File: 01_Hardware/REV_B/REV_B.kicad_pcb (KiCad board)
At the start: 2 copper layers, 65 x 30.5 mm, 6 parts, among them J1 Conn_02x20_Odd_Even, J2 RPi_GPIO, U1 MCP3004, U2 TB6612FNG

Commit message: Designing RevB
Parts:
- removed ? (x2): , RPi_Hat:RPi_Hat_Mounting_Hole
- added 100n1: C, Capacitor_SMD:C_0603_1608Metric, F.Cu at (44.2, 49.6)
- added C1: 10n, Capacitor_SMD:C_0603_1608Metric, F.Cu at (43.2, 65.6)
- added C10: 100n, Capacitor_SMD:C_0603_1608Metric, F.Cu at (25.6, 68.0)
- added C2: 10n, Capacitor_SMD:C_0603_1608Metric, F.Cu at (39.8, 65.6)
- added C3: 10n, Capacitor_SMD:C_0603_1608Metric, F.Cu at (21.8, 62.7)
- added C4: 10n, Capacitor_SMD:C_0603_1608Metric, F.Cu at (31.6, 59.3)
- added C5: 10n, Capacitor_SMD:C_0603_1608Metric, F.Cu at (43.3, 44.2)
- added C6: 10n, Capacitor_SMD:C_0603_1608Metric, F.Cu at (39.9, 49.6)
- added C7: 10n, Capacitor_SMD:C_0603_1608Metric, F.Cu at (25.1, 62.7)
- added C8: 10n, Capacitor_SMD:C_0603_1608Metric, F.Cu at (21.8, 68.0)
- added C9: 10u, Capacitor_SMD:CP_Elec_4x4.5, F.Cu at (33.5, 40.0)
- added J3: Conn_01x02, Connector_Molex:Molex_KK-254_AE-6410-02A_1x02_P2.54mm_Vertical, F.Cu at (61.2, 22.4)
- added J4: Conn_01x08_Male, Connector_PinHeader_2.54mm:PinHeader_1x08_P2.54mm_Vertical, F.Cu at (23.0, 38.8)
- added J5: Conn_01x08_Male, Connector_PinHeader_2.54mm:PinHeader_1x08_P2.54mm_Vertical, F.Cu at (9.20, 38.8)
- added R1: 10k, Resistor_SMD:R_0603_1608Metric, F.Cu at (53.5, 54.9)
- added R10: 1k, Resistor_SMD:R_0603_1608Metric, F.Cu at (32.9, 64.7)
- added R11: 1k, Resistor_SMD:R_0603_1608Metric, F.Cu at (58.7, 38.2)
- added R12: 1k, Resistor_SMD:R_0603_1608Metric, F.Cu at (39.9, 44.2)
- added R13: 1k, Resistor_SMD:R_0603_1608Metric, F.Cu at (69.1, 38.2)
- added R14: 22k, Resistor_SMD:R_0603_1608Metric, F.Cu at (38.4, 60.3)
- added R15: 22k, Resistor_SMD:R_0603_1608Metric, F.Cu at (41.9, 60.3)
- added R16: 22k, Resistor_SMD:R_0603_1608Metric, F.Cu at (32.9, 70.0)
- added R17: 22k, Resistor_SMD:R_0603_1608Metric, F.Cu at (52.0, 49.6)
- added R18: 10k, Resistor_SMD:R_0603_1608Metric, F.Cu at (46.7, 54.9)
- added R19: 10k, Resistor_SMD:R_0603_1608Metric, F.Cu at (62.2, 38.2)
- added R2: 1k, Resistor_SMD:R_0603_1608Metric, F.Cu at (46.7, 44.2)
- added R20: 10k, Resistor_SMD:R_0603_1608Metric, F.Cu at (56.9, 43.5)
- added R21: 10k, Resistor_SMD:R_0603_1608Metric, F.Cu at (60.3, 43.5)
- added R22: 10k, Resistor_SMD:R_0603_1608Metric, F.Cu at (65.6, 38.2)
- added R23: 10k, Resistor_SMD:R_0603_1608Metric, F.Cu at (36.4, 65.6)
- added R24: 10k, Resistor_SMD:R_0603_1608Metric, F.Cu at (29.5, 70.0)
- added R25: 10k, Resistor_SMD:R_0603_1608Metric, F.Cu at (36.4, 71.0)
- added R26: 10k, Resistor_SMD:R_0603_1608Metric, F.Cu at (48.6, 49.6)
- added R27: 10k, Resistor_SMD:R_0603_1608Metric, F.Cu at (63.8, 43.5)
- added R28: 10k, Resistor_SMD:R_0603_1608Metric, F.Cu at (56.9, 48.9)
- added R29: 10k, Resistor_SMD:R_0603_1608Metric, F.Cu at (50.1, 54.9)
- added R3: 1k, Resistor_SMD:R_0603_1608Metric, F.Cu at (55.3, 38.2)
- added R30: 10k, Resistor_SMD:R_0603_1608Metric, F.Cu at (45.3, 60.3)
- added R31: 10k, Resistor_SMD:R_0603_1608Metric, F.Cu at (60.3, 48.9)
- added R32: 10k, Resistor_SMD:R_0603_1608Metric, F.Cu at (48.8, 60.3)
- added R4: 1k, Resistor_SMD:R_0603_1608Metric, F.Cu at (29.5, 64.7)
- added R5: 1k, Resistor_SMD:R_0603_1608Metric, F.Cu at (50.1, 44.2)
- added R6: 10k, Resistor_SMD:R_0603_1608Metric, F.Cu at (39.9, 54.9)
- added R7: 10k, Resistor_SMD:R_0603_1608Metric, F.Cu at (35.0, 59.3)
- added R8: 10k, Resistor_SMD:R_0603_1608Metric, F.Cu at (43.3, 54.9)
- added R9: 10k, Resistor_SMD:R_0603_1608Metric, F.Cu at (53.5, 44.2)
- added U3: BSS138PS, Package_TO_SOT_SMD:SOT-363_SC-70-6, F.Cu at (34.1, 53.6)
- added U4: BSS138PS, Package_TO_SOT_SMD:SOT-363_SC-70-6, F.Cu at (34.1, 47.6)
- added U5: BSS138PS, Package_TO_SOT_SMD:SOT-363_SC-70-6, F.Cu at (41.2, 38.5)
- added U6: MCP3008, Package_SOIC:SOIC-16_3.9x9.9mm_P1.27mm, F.Cu at (6.21, 67.0)
- J1: value Conn_02x20_Odd_Even -> RaspberryPi; footprint Connector_PinHeader_2.54mm:PinHeader_2x20_P2.54mm_Vertical -> Connector_PinSocket_2.54mm:PinSocket_2x20_P2.54mm_Vertical
- J2: value RPi_GPIO -> Conn_01x02; footprint RPi_Hat:Pin_Header_Straight_2x20 -> Connector_Molex:Molex_KK-254_AE-6410-02A_1x02_P2.54mm_Vertical
- U1: value MCP3004 -> TB6612FNG; footprint Package_SSOP:TSSOP-14_4.4x5mm_P0.65mm -> Package_SSOP:SSOP-24_5.3x8.2mm_P0.65mm
- U2: value TB6612FNG -> BSS138PS; footprint Package_SSOP:SSOP-24_5.3x8.2mm_P0.65mm -> Package_TO_SOT_SMD:SOT-363_SC-70-6
- moved J1 140.6 mm to (8.37, 2.28)
- moved U2 127.6 mm to (49.5, 38.5)
- moved U1 107.9 mm to (15.1, 66.3)
- moved J2 105.9 mm to (61.2, 14.5), turned to 270 degrees
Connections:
- J1 pad 10: /GPIO15 -> Net-(J1-Pad10)
- J1 pad 11: /GPIO17 -> Net-(J1-Pad11)
- J1 pad 12: /GPIO18 -> Net-(J1-Pad12)
- J1 pad 13: /GPIO27 -> Net-(J1-Pad13)
- J1 pad 15: /GPIO22 -> Net-(J1-Pad15)
- J1 pad 16: /GPIO23 -> Net-(J1-Pad16)
- J1 pad 18: /GPIO24 -> Net-(J1-Pad18)
- J1 pad 19: /GPIO10 -> Net-(J1-Pad19)
- J1 pad 21: /GPIO9 -> Net-(J1-Pad21)
- J1 pad 22: /GPIO25 -> Net-(J1-Pad22)
- J1 pad 23: /GPIO11 -> Net-(J1-Pad23)
- J1 pad 24: /GPIO8 -> Net-(J1-Pad24)
- J1 pad 26: /GPIO7 -> Net-(J1-Pad26)
- J1 pad 27: (no net) -> Net-(J1-Pad27)
- J1 pad 28: (no net) -> Net-(J1-Pad28)
- J1 pad 29: /GPIO5 -> Net-(J1-Pad29)
- J1 pad 3: /GPIO2 -> IC21_SDA
- J1 pad 31: /GPIO6 -> Net-(J1-Pad31)
- J1 pad 32: /GPIO12 -> Net-(J1-Pad32)
- J1 pad 33: /GPIO13 -> Net-(J1-Pad33)
- J1 pad 35: /GPIO19 -> Net-(J1-Pad35)
- J1 pad 36: /GPIO16 -> Net-(J1-Pad36)
- J1 pad 37: /GPIO26 -> Net-(J1-Pad37)
- J1 pad 38: /GPIO20 -> Net-(J1-Pad38)
- J1 pad 40: /GPIO21 -> Net-(J1-Pad40)
- J1 pad 5: /GPIO3 -> I2C1_SCL
- J1 pad 7: /GPIO4 -> Net-(J1-Pad7)
- J1 pad 8: /GPIO14 -> Net-(J1-Pad8)
- J2 pad 1: +3V3 -> Net-(J2-Pad1)
- J2 pad 2: +5V -> Net-(J2-Pad2)
- U1 pad 1: (no net) -> Net-(J2-Pad1)
- U1 pad 10: (no net) -> GND
- U1 pad 11: (no net) -> Net-(J3-Pad1)
- U1 pad 12: (no net) -> Net-(J3-Pad1)
- U1 pad 13: (no net) -> +BATT
- U1 pad 14: (no net) -> +BATT
- U1 pad 2: (no net) -> Net-(J2-Pad1)
- U1 pad 3: (no net) -> GND
- U1 pad 4: (no net) -> GND
- U1 pad 5: (no net) -> Net-(J2-Pad2)
- U1 pad 6: (no net) -> Net-(J2-Pad2)
- U1 pad 7: (no net) -> Net-(J3-Pad2)
- U1 pad 8: (no net) -> Net-(J3-Pad2)
- U1 pad 9: (no net) -> GND
- U2 pad 1: (no net) -> IC21_SDA
- U2 pad 2: (no net) -> +3V3
- U2 pad 3: (no net) -> Net-(J5-Pad2)
- U2 pad 4: (no net) -> I2C1_SCL
- U2 pad 5: (no net) -> +3V3
- U2 pad 6: (no net) -> Net-(J5-Pad1)
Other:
- board size 65 x 30.5 mm -> 65 x 30 mm
- net class Default: via_dia 0.6 -> 0.8
- rule pad_to_mask_clearance: 0 -> 0.2
- rule trace_min: 0.01 -> 0.2

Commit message: Work in Progress
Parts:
- removed U4: BSS138PS, Package_TO_SOT_SMD:SOT-363_SC-70-6
- added J10: Conn_01x03, Connector_PinHeader_2.54mm:PinHeader_1x03_P2.54mm_Vertical, F.Cu at (36.8, 21.8)
- added J11: Conn_01x03, Connector_PinHeader_2.54mm:PinHeader_1x03_P2.54mm_Vertical, F.Cu at (54.9, -19.8)
- added J12: Conn_01x03, Connector_PinHeader_2.54mm:PinHeader_1x03_P2.54mm_Vertical, F.Cu at (48.3, 21.8)
- added J13: Conn_01x03, Connector_PinHeader_2.54mm:PinHeader_1x03_P2.54mm_Vertical, F.Cu at (51.8, 21.8)
- added J14: Conn_01x03, Connector_PinHeader_2.54mm:PinHeader_1x03_P2.54mm_Vertical, F.Cu at (55.4, 21.8)
- added J15: Conn_01x03, Connector_PinHeader_2.54mm:PinHeader_1x03_P2.54mm_Vertical, F.Cu at (40.4, 21.8)
- added J16: Conn_01x08_Male, Connector_PinHeader_2.54mm:PinHeader_1x03_P2.54mm_Vertical, F.Cu at (43.9, 21.8)
- added J6: Conn_01x03, Connector_PinHeader_2.54mm:PinHeader_1x03_P2.54mm_Vertical, F.Cu at (22.4, 21.8)
- added J7: Conn_01x03, Connector_PinHeader_2.54mm:PinHeader_1x03_P2.54mm_Vertical, F.Cu at (25.7, 21.8)
- added J8: Conn_01x03, Connector_PinHeader_2.54mm:PinHeader_1x03_P2.54mm_Vertical, F.Cu at (29.2, 21.8)
- added J9: Conn_01x03, Connector_PinHeader_2.54mm:PinHeader_1x03_P2.54mm_Vertical, F.Cu at (33.3, 21.8)
- added U7: BSS138PS, Package_SSOP:TSSOP-28_4.4x9.7mm_P0.65mm, B.Cu at (41.7, 14.5)
- added U8: BSS138PS, Package_TO_SOT_SMD:SOT-363_SC-70-6, F.Cu at (63.8, -20.2)
- C1: value 10n -> 10u
- C10: value 100n -> 10n
- C2: value 10n -> 100n
- C9: value 10u -> 10n
- J4: value Conn_01x08_Male -> Conn_01x02
- R1, R9: value 10k -> 1k
- R13: value 1k -> 22k
- R17: value 22k -> 10k
- R5: value 1k -> 10k
- U2: value BSS138PS -> MCP3008
- U3: value BSS138PS -> PCA9685PW
- U6: value MCP3008 -> BSS138PS
- moved R16 79.4 mm to (70.1, -0.14), turned to 90 degrees
- moved C8 75.6 mm to (76.7, 16.0), turned to 90 degrees
- moved C10 75.0 mm to (76.6, 13.0), turned to 90 degrees
- moved R15 70.7 mm to (72.5, -3.51), turned to 90 degrees
- moved C3 69.9 mm to (74.6, 16.8), turned to 90 degrees
- moved C7 69.8 mm to (74.6, 13.5), turned to 90 degrees
- moved R14 69.3 mm to (72.5, -0.06), turned to 90 degrees
- moved R7 67.5 mm to (72.3, 3.10), turned to 90 degrees
- moved C4 66.7 mm to (72.3, 6.47), turned to 90 degrees
- moved R25 64.9 mm to (6.22, 13.5), turned to 180 degrees
- moved R30 63.4 mm to (6.22, 10.4), turned to 180 degrees
- moved R27 62.4 mm to (6.22, 19.3), turned to 180 degrees
- moved U1 61.6 mm to (47.8, 14.0), turned to 180 degrees
- moved R4 61.0 mm to (74.6, 23.6), turned to 90 degrees
- moved R10 61.0 mm to (74.6, 20.2), turned to 90 degrees
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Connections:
- C1 pad 1: Net-(C1-Pad1) -> +BATT
- C10 pad 1: +BATT -> Net-(C10-Pad1)
- C2 pad 1: Net-(C2-Pad1) -> +BATT
- C9 pad 1: +BATT -> Net-(C9-Pad1)
- J1 pad 10: Net-(J1-Pad10) -> (no net)
- J1 pad 11: Net-(J1-Pad11) -> (no net)
- J1 pad 12: Net-(J1-Pad12) -> (no net)
- J1 pad 13: Net-(J1-Pad13) -> (no net)
- J1 pad 15: Net-(J1-Pad15) -> (no net)
- J1 pad 16: Net-(J1-Pad16) -> (no net)
- J1 pad 18: Net-(J1-Pad18) -> (no net)
- J1 pad 19: Net-(J1-Pad19) -> (no net)
- J1 pad 21: Net-(J1-Pad21) -> (no net)
- J1 pad 22: Net-(J1-Pad22) -> (no net)
- J1 pad 23: Net-(J1-Pad23) -> (no net)
- J1 pad 24: Net-(J1-Pad24) -> (no net)
- J1 pad 26: Net-(J1-Pad26) -> (no net)
- J1 pad 27: Net-(J1-Pad27) -> (no net)
- J1 pad 28: Net-(J1-Pad28) -> (no net)
- J1 pad 29: Net-(J1-Pad29) -> (no net)
- J1 pad 3: IC21_SDA -> (no net)
- J1 pad 31: Net-(J1-Pad31) -> (no net)
- J1 pad 5: I2C1_SCL -> (no net)
- J1 pad 7: Net-(J1-Pad7) -> (no net)
- J1 pad 8: Net-(J1-Pad8) -> (no net)
- J2 pad 1: Net-(J2-Pad1) -> +BATT
- J2 pad 2: Net-(J2-Pad2) -> GND
- J4 pad 3: Net-(J4-Pad3) -> (no net)
- J4 pad 4: Net-(J4-Pad4) -> (no net)
- J4 pad 5: Net-(J4-Pad5) -> (no net)
- J4 pad 6: Net-(J4-Pad6) -> (no net)
- J4 pad 7: Net-(J4-Pad7) -> (no net)
- J4 pad 8: Net-(J4-Pad8) -> (no net)
- R1 pad 1: +3V3 -> Net-(C3-Pad1)
- R1 pad 2: Net-(R1-Pad2) -> GND
- R10 pad 1: Net-(J4-Pad1) -> Net-(J5-Pad2)
- R10 pad 2: Net-(C1-Pad1) -> Net-(C4-Pad1)
- R11 pad 1: Net-(J4-Pad2) -> Net-(J5-Pad3)
- R11 pad 2: Net-(C2-Pad1) -> Net-(C5-Pad1)
- R12 pad 1: Net-(J4-Pad3) -> Net-(J5-Pad4)
- R12 pad 2: Net-(C3-Pad1) -> Net-(C6-Pad1)
- R13 pad 1: Net-(J4-Pad4) -> Net-(J5-Pad5)
- R13 pad 2: Net-(C4-Pad1) -> Net-(C7-Pad1)
- R14 pad 1: Net-(J4-Pad5) -> Net-(J5-Pad6)
- R14 pad 2: Net-(C5-Pad1) -> Net-(C8-Pad1)
- R15 pad 1: Net-(J4-Pad6) -> Net-(J5-Pad7)
- R15 pad 2: Net-(C6-Pad1) -> Net-(C9-Pad1)
- R16 pad 1: Net-(J4-Pad7) -> Net-(J5-Pad8)
- R16 pad 2: Net-(C7-Pad1) -> Net-(C10-Pad1)
- R17 pad 1: Net-(J4-Pad8) -> +3V3
- R17 pad 2: Net-(C8-Pad1) -> Net-(R17-Pad2)
- R19 pad 2: IC21_SDA -> Net-(R19-Pad2)
- R2 pad 1: Net-(C1-Pad1) -> Net-(C4-Pad1)
- R20 pad 2: I2C1_SCL -> Net-(R20-Pad2)
- R25 pad 2: Net-(J5-Pad3) -> Net-(J16-Pad3)
- R26 pad 2: Net-(J5-Pad1) -> Net-(J16-Pad1)
- R27 pad 2: Net-(J5-Pad5) -> Net-(J16-Pad5)
- R28 pad 2: Net-(J5-Pad7) -> Net-(J16-Pad7)
- R29 pad 2: Net-(J5-Pad4) -> Net-(J16-Pad4)
- R3 pad 1: Net-(C2-Pad1) -> Net-(C5-Pad1)
- R30 pad 2: Net-(J5-Pad2) -> Net-(J16-Pad2)
- R31 pad 2: Net-(J5-Pad6) -> Net-(J16-Pad6)
- R32 pad 2: Net-(J5-Pad8) -> Net-(J16-Pad8)
- R4 pad 1: Net-(C3-Pad1) -> Net-(C6-Pad1)
- R5 pad 1: Net-(C4-Pad1) -> Net-(C7-Pad1)
- R6 pad 1: Net-(C5-Pad1) -> Net-(C8-Pad1)
- R7 pad 1: Net-(C6-Pad1) -> Net-(C9-Pad1)
- R8 pad 1: Net-(C7-Pad1) -> Net-(C10-Pad1)
- R9 pad 1: Net-(C8-Pad1) -> Net-(J5-Pad1)
- R9 pad 2: GND -> Net-(C3-Pad1)
- U1 pad 1: Net-(J2-Pad1) -> Net-(J3-Pad1)
- U1 pad 11: Net-(J3-Pad1) -> Net-(J4-Pad1)
- U1 pad 12: Net-(J3-Pad1) -> Net-(J4-Pad1)
- U1 pad 2: Net-(J2-Pad1) -> Net-(J3-Pad1)
- U1 pad 5: Net-(J2-Pad2) -> Net-(J3-Pad2)
- U1 pad 6: Net-(J2-Pad2) -> Net-(J3-Pad2)
- U1 pad 7: Net-(J3-Pad2) -> Net-(J4-Pad2)
- U1 pad 8: Net-(J3-Pad2) -> Net-(J4-Pad2)
- U2 pad 1: IC21_SDA -> Net-(C3-Pad1)
- U2 pad 2: +3V3 -> Net-(C4-Pad1)
- U2 pad 3: Net-(J5-Pad2) -> Net-(C5-Pad1)
- U2 pad 4: I2C1_SCL -> Net-(C6-Pad1)
- U2 pad 5: +3V3 -> Net-(C7-Pad1)
- U2 pad 6: Net-(J5-Pad1) -> Net-(C8-Pad1)
- U3 pad 1: Net-(R1-Pad2) -> (no net)
- U3 pad 2: +3V3 -> (no net)
- U3 pad 3: Net-(J5-Pad4) -> (no net)
- U3 pad 4: Net-(R18-Pad2) -> (no net)
- U3 pad 5: +3V3 -> (no net)
- U3 pad 6: Net-(J5-Pad3) -> Net-(J6-Pad1)
- U5 pad 1: Net-(R23-Pad2) -> Net-(R17-Pad2)
- U5 pad 3: Net-(J5-Pad8) -> Net-(J16-Pad4)
- U5 pad 4: Net-(R24-Pad2) -> Net-(R18-Pad2)
- U5 pad 6: Net-(J5-Pad7) -> Net-(J16-Pad3)
- U6 pad 1: Net-(C1-Pad1) -> Net-(R19-Pad2)
- U6 pad 10: Net-(J1-Pad24) -> (no net)
- U6 pad 11: Net-(J1-Pad19) -> (no net)
- U6 pad 12: Net-(J1-Pad21) -> (no net)
- U6 pad 13: Net-(J1-Pad23) -> (no net)
- U6 pad 14: GND -> (no net)
- U6 pad 15: +3V3 -> (no net)
- U6 pad 16: +3V3 -> (no net)
- U6 pad 2: Net-(C2-Pad1) -> +3V3
- U6 pad 3: Net-(C3-Pad1) -> Net-(J16-Pad2)
- U6 pad 4: Net-(C4-Pad1) -> Net-(R20-Pad2)
- U6 pad 5: Net-(C5-Pad1) -> +3V3
- U6 pad 6: Net-(C6-Pad1) -> Net-(J16-Pad1)
- U6 pad 7: Net-(C7-Pad1) -> (no net)
- U6 pad 8: Net-(C8-Pad1) -> (no net)
- U6 pad 9: GND -> (no net)
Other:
- board text added: "x = 8,37 y = 2,278"

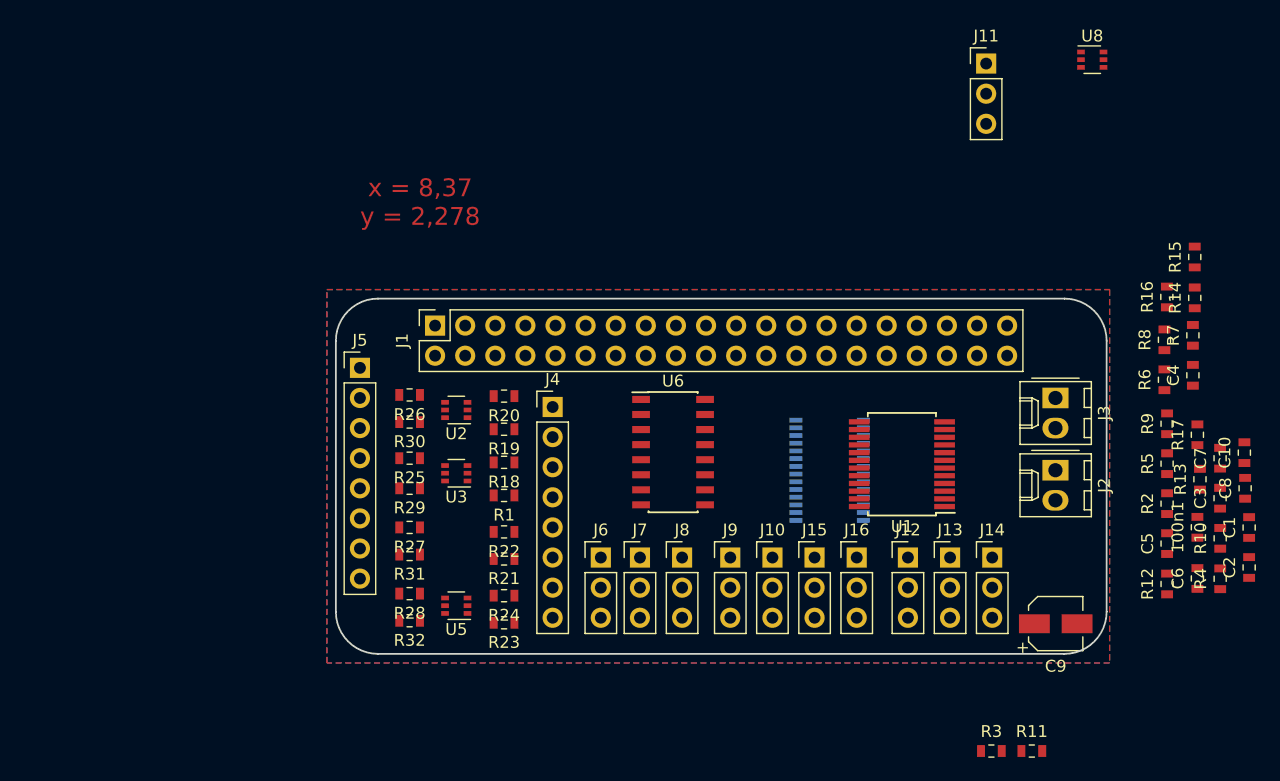
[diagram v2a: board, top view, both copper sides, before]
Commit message: Brd redo due to kicad update
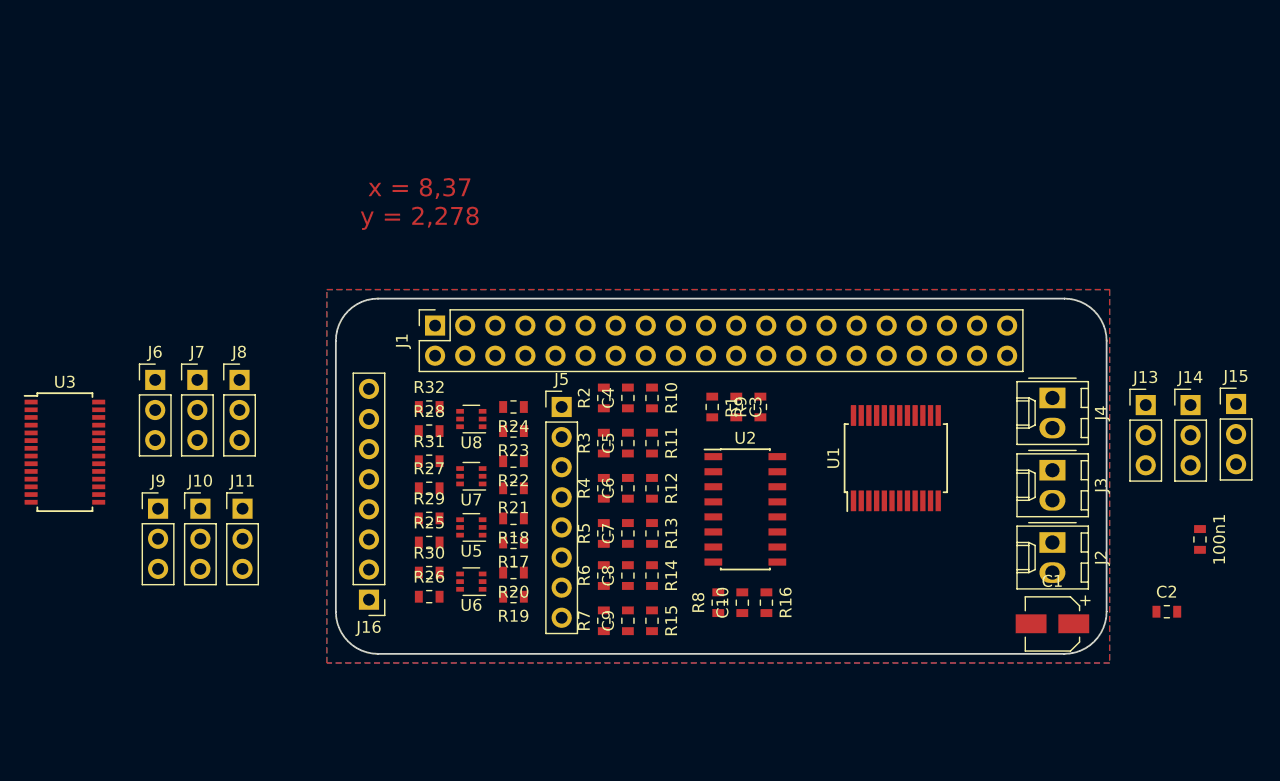
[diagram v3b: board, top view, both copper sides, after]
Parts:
- removed J12: Conn_01x03, Connector_PinHeader_2.54mm:PinHeader_1x03_P2.54mm_Vertical
- C1: footprint Capacitor_SMD:C_0603_1608Metric -> Capacitor_SMD:CP_Elec_4x4.5
- C9: footprint Capacitor_SMD:CP_Elec_4x4.5 -> Capacitor_SMD:C_0603_1608Metric
- J16: footprint Connector_PinHeader_2.54mm:PinHeader_1x03_P2.54mm_Vertical -> Connector_PinHeader_2.54mm:PinHeader_1x08_P2.54mm_Vertical
- J4: footprint Connector_PinHeader_2.54mm:PinHeader_1x08_P2.54mm_Vertical -> Connector_Molex:Molex_KK-254_AE-6410-02A_1x02_P2.54mm_Vertical
- U1: footprint Package_SSOP:SSOP-24_5.3x8.2mm_P0.65mm -> Package_SO:SSOP-24_5.3x8.2mm_P0.65mm
- U2: footprint Package_TO_SOT_SMD:SOT-363_SC-70-6 -> Package_SO:SOIC-16_3.9x9.9mm_P1.27mm
- U3: footprint Package_TO_SOT_SMD:SOT-363_SC-70-6 -> Package_SO:TSSOP-28_4.4x9.7mm_P0.65mm
- U6: footprint Package_SOIC:SOIC-16_3.9x9.9mm_P1.27mm -> Package_TO_SOT_SMD:SOT-363_SC-70-6
- U7: footprint Package_SSOP:TSSOP-28_4.4x9.7mm_P0.65mm -> Package_TO_SOT_SMD:SOT-363_SC-70-6; moved to F.Cu
- moved J11 73.1 mm to (-7.87, 17.7)
- moved U8 60.5 mm to (11.4, 10.2), turned to 180 degrees
- moved R17 58.4 mm to (15.0, 20.6), turned to 180 degrees
- moved R7 55.2 mm to (22.6, 27.2)
- moved R15 55.1 mm to (26.7, 27.2), turned to 270 degrees
- moved C8 52.6 mm to (24.6, 23.4)
- moved R4 52.6 mm to (22.6, 16.0)
- moved R14 51.4 mm to (26.7, 23.4), turned to 270 degrees
- moved C7 50.4 mm to (24.6, 19.8)
- moved R6 50.1 mm to (22.6, 23.4)
- moved R10 49.4 mm to (26.7, 8.38), turned to 270 degrees
- moved C6 48.6 mm to (24.6, 16.0)
- moved J9 48.4 mm to (-15.0, 17.7)
- moved J10 48.4 mm to (-11.4, 17.7)
- moved R2 48.3 mm to (22.6, 8.38)
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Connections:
- J1 pad 19: (no net) -> Net-(J1-Pad19)
- J1 pad 21: (no net) -> Net-(J1-Pad21)
- J1 pad 23: (no net) -> Net-(J1-Pad23)
- J1 pad 24: (no net) -> Net-(J1-Pad24)
- J1 pad 38: Net-(J1-Pad38) -> (no net)
- J10 pad 1: (no net) -> Net-(J10-Pad1)
- J11 pad 1: (no net) -> Net-(J11-Pad1)
- J6 pad 2: (no net) -> Net-(J6-Pad2)
- J6 pad 3: (no net) -> Net-(J6-Pad3)
- J7 pad 1: (no net) -> Net-(J7-Pad1)
- J7 pad 2: (no net) -> Net-(J7-Pad2)
- J7 pad 3: (no net) -> Net-(J7-Pad3)
- J8 pad 1: (no net) -> Net-(J8-Pad1)
- J8 pad 2: (no net) -> Net-(J8-Pad2)
- J8 pad 3: (no net) -> Net-(J8-Pad3)
- J9 pad 1: (no net) -> Net-(J9-Pad1)
- U1 pad 16: Net-(J1-Pad38) -> (no net)
